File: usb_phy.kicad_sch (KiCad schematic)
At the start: 14 parts, among them U8 USB3343-CP

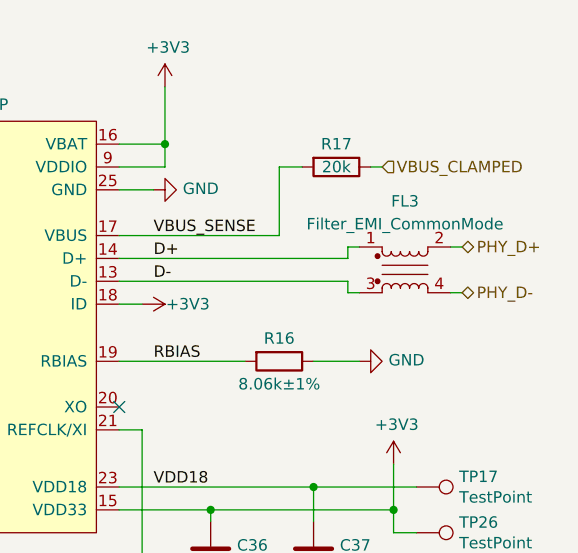
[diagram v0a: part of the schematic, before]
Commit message: Upgrade to KiCad 7
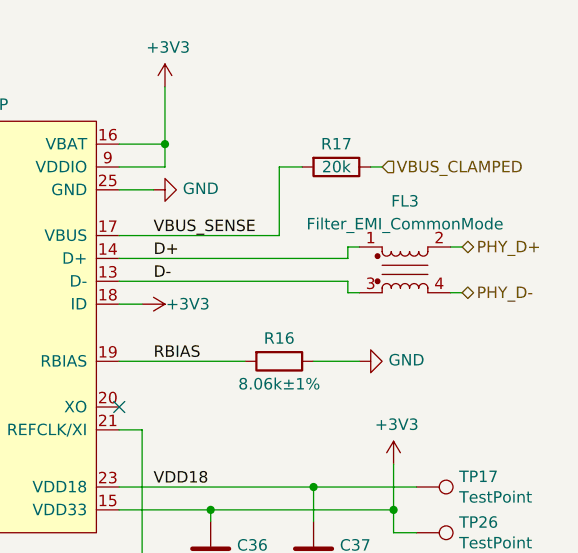
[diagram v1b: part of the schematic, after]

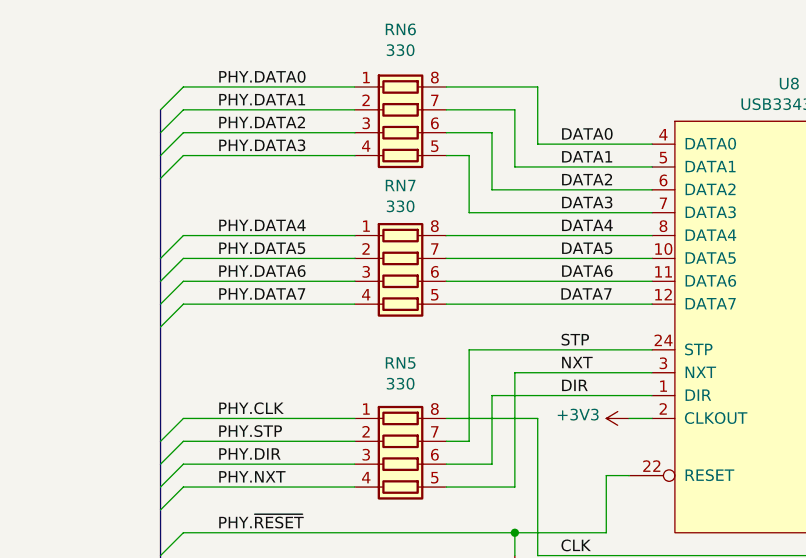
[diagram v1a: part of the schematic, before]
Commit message: Replace ULPI series resistors with 0 ohms
Tests indicate that these resistors do not reduce emissions, but we're
changing them to zero ohms and keeping them for now just in case.
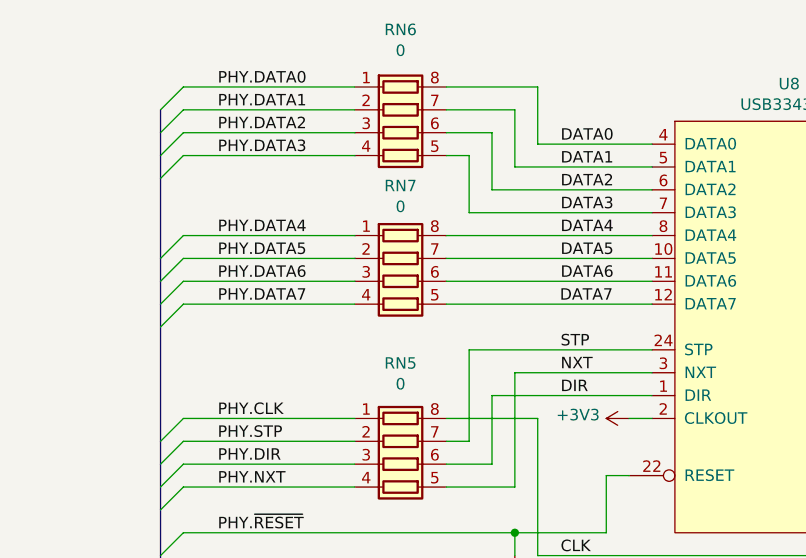
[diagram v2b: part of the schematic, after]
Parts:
- RN5, RN6, RN7: value 330 -> 0; Part Number YC124-JR-07330RL -> YC124-JR-070RL
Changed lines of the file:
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@@
       (effects (font (size 1.27 1.27)))
     )
-    (property "Value" "330" (at 113.03 66.6496 90)
+    (property "Value" "0" (at 113.03 66.6496 90)
       (effects (font (size 1.27 1.27)))
     )
@@
       (effects (font (size 1.27 1.27)) hide)
     )
-    (property "Description" "RES ARRAY 4 RES 330 OHM 0804" (at 113.03 74.93 0)
+    (property "Description" "RES ARRAY 4 RES ZERO OHM 0804" (at 113.03 74.93 0)
       (effects (font (size 1.27 1.27)) hide)
     )
@@
       (effects (font (size 1.27 1.27)) hide)
     )
-    (property "Part Number" "YC124-JR-07330RL" (at 113.03 74.93 0)
+    (property "Part Number" "YC124-JR-070RL" (at 113.03 74.93 0)
       (effects (font (size 1.27 1.27)) hide)
     )
@@
       (effects (font (size 1.27 1.27)))
     )
-    (property "Value" "330" (at 113.03 49.3014 90)
+    (property "Value" "0" (at 113.03 49.3014 90)
       (effects (font (size 1.27 1.27)))
     )
@@
       (effects (font (size 1.27 1.27)) hide)
     )
-    (property "Description" "RES ARRAY 4 RES 330 OHM 0804" (at 113.03 58.42 0)
+    (property "Description" "RES ARRAY 4 RES ZERO OHM 0804" (at 113.03 58.42 0)
       (effects (font (size 1.27 1.27)) hide)
     )
@@
       (effects (font (size 1.27 1.27)) hide)
     )
-    (property "Part Number" "YC124-JR-07330RL" (at 113.03 58.42 0)
+    (property "Part Number" "YC124-JR-070RL" (at 113.03 58.42 0)
       (effects (font (size 1.27 1.27)) hide)
     )
@@
       (effects (font (size 1.27 1.27)))
     )
-    (property "Value" "330" (at 113.03 86.36 90)
+    (property "Value" "0" (at 113.03 86.36 90)
       (effects (font (size 1.27 1.27)))
     )
@@
       (effects (font (size 1.27 1.27)) hide)
     )
-    (property "Description" "RES ARRAY 4 RES 330 OHM 0804" (at 113.03 95.25 0)
+    (property "Description" "RES ARRAY 4 RES ZERO OHM 0804" (at 113.03 95.25 0)
       (effects (font (size 1.27 1.27)) hide)
     )
@@
       (effects (font (size 1.27 1.27)) hide)
     )
-    (property "Part Number" "YC124-JR-07330RL" (at 113.03 95.25 0)
-      (effects (font (size 1.27 1.27)) hide)
-    )
+    (property "Part Number" "YC124-JR-070RL" (at 113.03 95.25 0)
+      (effects (font (size 1.27 1.27)) hide)
+    )

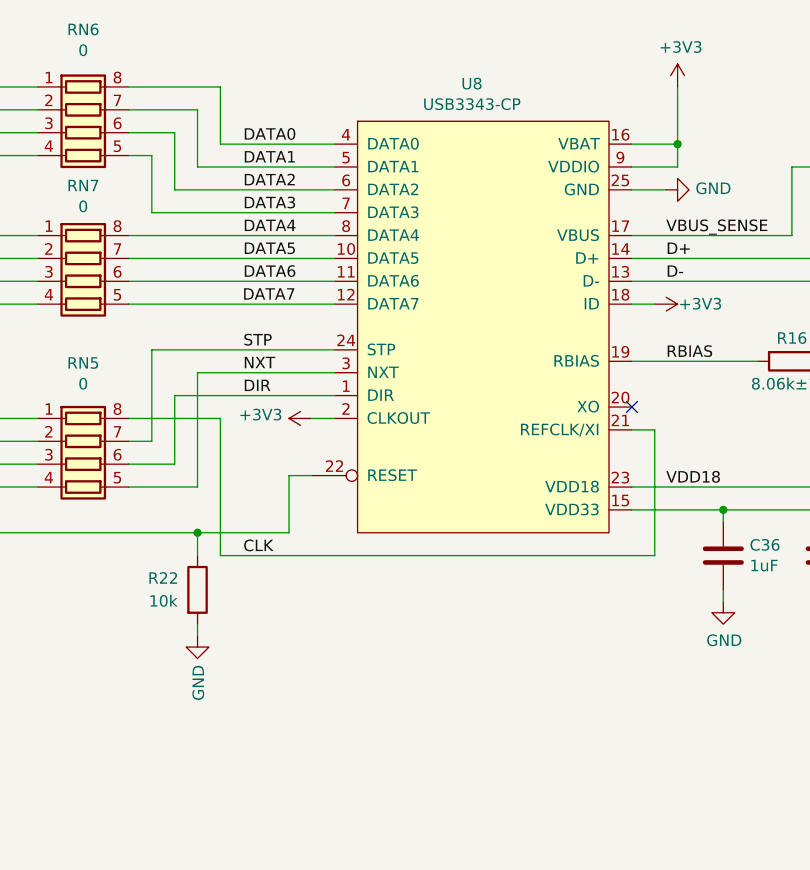
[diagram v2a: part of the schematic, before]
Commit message: Clean up schematic
- Renumber Pmod signal names to match silkscreen labels
- Clean up FPGA symbol
- Clean up PHY symbol
- Add title block to newer sheets
- Fix horizontal line in LED sheet
- Improve various label positions
- Update data sheet fields
- Renumber pages
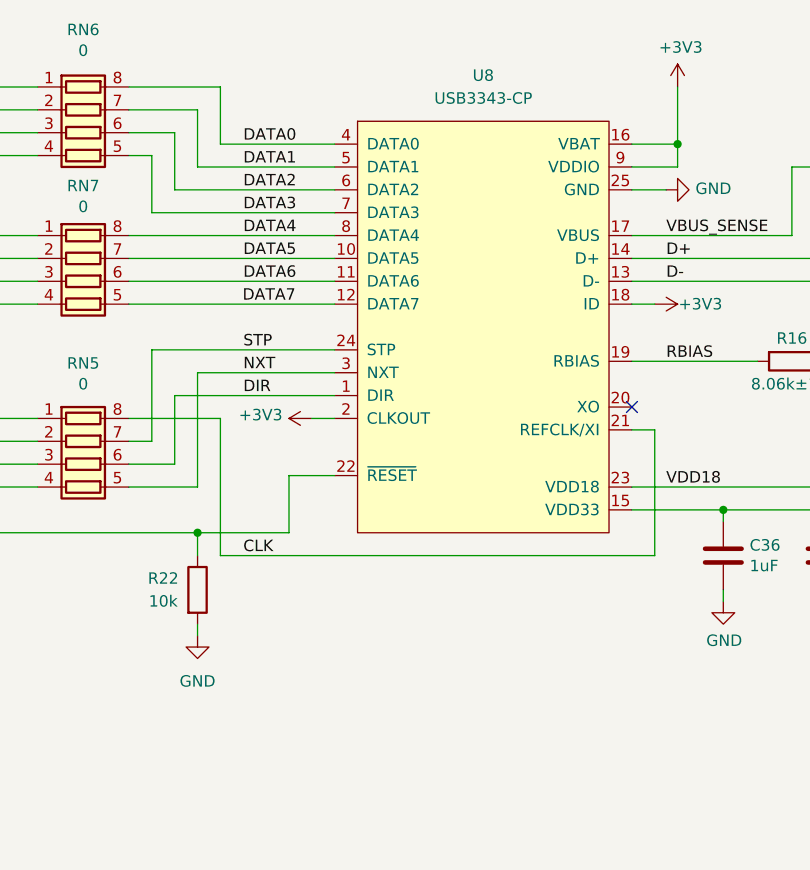
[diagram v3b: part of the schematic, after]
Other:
- company: (none) -> Copyright 2019-2023 Great Scott Gadgets
- title: (none) -> Cynthion
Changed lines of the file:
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@@
 (kicad_sch (version 20230121) (generator eeschema)
   (paper "A4")
+  (title_block
+    (title "Cynthion")
+    (date "${DATE}")
+    (rev "${VERSION}")
+    (company "Copyright 2019-2023 Great Scott Gadgets")
+    (comment 1 "Licensed under the CERN-OHL-P v2")
+  )
   (junction (at 179.07 59.69) (diameter 0) (color 0 0 0 0)
   )
@@
     (stroke (width 0) (type default))
   )
-  (wire (pts (xy 138.43 96.52) (xy 135.89 96.52))
+  (wire (pts (xy 140.97 96.52) (xy 135.89 96.52))
     (stroke (width 0) (type default))
   )
@@
     )
   )
-  (symbol (lib_id "usb:USB3343") (at 140.97 57.15 0) (unit 1)
-    (in_bom yes) (on_board yes) (dnp no)
-    (property "Reference" "U8" (at 156.21 53.0098 0)
-      (effects (font (size 1.27 1.27)))
-    )
-    (property "Value" "USB3343-CP" (at 156.21 55.2958 0)
-      (effects (font (size 1.27 1.27)))
-    )
-    (property "Footprint" "Package_DFN_QFN:VQFN-24-1EP_4x4mm_P0.5mm_EP2.45x2.45mm" (at 140.97 57.15 0)
-      (effects (font (size 1.27 1.27)) hide)
-    )
-    (property "Datasheet" "http://ww1.microchip.com/downloads/en/DeviceDoc/334x.pdf" (at 140.97 57.15 0)
-      (effects (font (size 1.27 1.27)) hide)
-    )
-    (property "Description" "IC TRANSCEIVER 1/1 24QFN" (at 140.97 57.15 0)
-      (effects (font (size 1.27 1.27)) hide)
-    )
-    (property "Manufacturer" "Microchip" (at 140.97 57.15 0)
-      (effects (font (size 1.27 1.27)) hide)
-    )
-    (property "Part Number" "USB3343-CP" (at 140.97 57.15 0)
+  (symbol (lib_id "usb:USB3343") (at 157.48 80.01 0) (unit 1)
+    (in_bom yes) (on_board yes) (dnp no) (fields_autoplaced)
+    (property "Reference" "U8" (at 157.48 52.07 0)
+      (effects (font (size 1.27 1.27)))
+    )
+    (property "Value" "USB3343-CP" (at 157.48 54.61 0)
+      (effects (font (size 1.27 1.27)))
+    )
+    (property "Footprint" "Package_DFN_QFN:VQFN-24-1EP_4x4mm_P0.5mm_EP2.45x2.45mm" (at 157.48 80.01 0)
+      (effects (font (size 1.27 1.27)) hide)
+    )
+    (property "Datasheet" "http://ww1.microchip.com/downloads/en/DeviceDoc/334x.pdf" (at 157.48 80.01 0)
+      (effects (font (size 1.27 1.27)) hide)
+    )
+    (property "Description" "IC TRANSCEIVER 1/1 24QFN" (at 157.48 80.01 0)
+      (effects (font (size 1.27 1.27)) hide)
+    )
+    (property "Manufacturer" "Microchip" (at 157.48 80.01 0)
+      (effects (font (size 1.27 1.27)) hide)
+    )
+    (property "Part Number" "USB3343-CP" (at 157.48 80.01 0)
       (effects (font (size 1.27 1.27)) hide)
     )
@@
       (effects (font (size 1.27 1.27)) hide)
     )
-    (property "Value" "GND" (at 125.857 117.5512 90)
-      (effects (font (size 1.27 1.27)) (justify right))
+    (property "Value" "GND" (at 125.73 119.38 0)
+      (effects (font (size 1.27 1.27)))
     )
     (property "Footprint" "" (at 125.73 114.3 0)

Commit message: Update common-mode choke part selection
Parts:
- FL3: Part Number DLM0NSN900HY2D -> DLM0NSB280HY2D
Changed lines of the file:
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@@
       (effects (font (size 1.27 1.27)) hide)
     )
-    (property "Description" "CMC 100MA 2LN 90 OHM SMD" (at 205.74 73.66 0)
+    (property "Description" "CMC 130MA 2LN 28 OHM SMD" (at 205.74 73.66 0)
       (effects (font (size 1.27 1.27)) hide)
     )
@@
       (effects (font (size 1.27 1.27)) hide)
     )
-    (property "Part Number" "DLM0NSN900HY2D" (at 205.74 73.66 0)
+    (property "Part Number" "DLM0NSB280HY2D" (at 205.74 73.66 0)
       (effects (font (size 1.27 1.27)) hide)
     )
